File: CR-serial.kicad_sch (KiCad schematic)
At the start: 26 parts, among them J1 USB, J2 GPIO, J3 UART0, J4 UART1, J5 UART2, J6 UART3_HV, J7 RS232_0, J8 RS232_1, U1 CP2108-xxx-xM, U2 MAX232

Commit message: Make GPIO header double-row
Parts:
- J2: footprint Connector_PinHeader_2.54mm:PinHeader_1x16_P2.54mm_Vertical -> Connector_PinHeader_2.54mm:PinHeader_2x08_P2.54mm_Vertical
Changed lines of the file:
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@@
 			)
 		)
-		(property "Footprint" "Connector_PinHeader_2.54mm:PinHeader_1x16_P2.54mm_Vertical"
+		(property "Footprint" "Connector_PinHeader_2.54mm:PinHeader_2x08_P2.54mm_Vertical"
 			(at 67.31 118.11 0)
 			(effects

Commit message: Change RS232 connectors
Zones filled again
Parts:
- J7, J8: footprint Connector_PinHeader_2.54mm:PinHeader_1x03_P2.54mm_Vertical -> Connector_Phoenix_MC:PhoenixContact_MCV_1,5_3-G-3.81_1x03_P3.81mm_Vertical
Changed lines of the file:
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@@
 			)
 		)
-		(property "Footprint" "Connector_PinHeader_2.54mm:PinHeader_1x03_P2.54mm_Vertical"
+		(property "Footprint" "Connector_Phoenix_MC:PhoenixContact_MCV_1,5_3-G-3.81_1x03_P3.81mm_Vertical"
 			(at 259.08 88.9 0)
 			(effects
@@
 			)
 		)
-		(property "Footprint" "Connector_PinHeader_2.54mm:PinHeader_1x03_P2.54mm_Vertical"
+		(property "Footprint" "Connector_Phoenix_MC:PhoenixContact_MCV_1,5_3-G-3.81_1x03_P3.81mm_Vertical"
 			(at 259.08 101.6 0)
 			(effects

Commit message: Refactor UARTs: move GND next to TX/RX
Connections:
- net RX0: now also J3.3 (Pin_3); no longer J3.8 (Pin_8)
- net RX1: now also J4.3 (Pin_3); no longer J4.8 (Pin_8)
- net TX0: now also J3.2 (Pin_2); no longer J3.9 (Pin_9)
- net TX1: now also J4.2 (Pin_2); no longer J4.9 (Pin_9)
- net at U1.1 (RX3): now also J6.3 (Pin_3); no longer J6.8 (Pin_8)
- net at U1.10 (~{DTR3}): now also J6.6 (Pin_6); no longer J6.5 (Pin_5)
- net at U1.11 (~{RI2}): now also J5.9 (Pin_9); no longer J5.2 (Pin_2)
- net at U1.12 (~{DCD2}): now also J5.8 (Pin_8); no longer J5.3 (Pin_3)
- net at U1.13 (~{CTS2}): now also J5.5 (Pin_5); no longer J5.6 (Pin_6)
- net at U1.14 (~{RTS2}): now also J5.4 (Pin_4); no longer J5.7 (Pin_7)
- net at U1.15 (RX2): now also J5.3 (Pin_3); no longer J5.8 (Pin_8)
- net at U1.16 (TX2): now also J5.2 (Pin_2); no longer J5.9 (Pin_9)
- net at U1.17 (~{DSR2}): now also J5.7 (Pin_7); no longer J5.4 (Pin_4)
- net at U1.18 (~{DTR2}): now also J5.6 (Pin_6); no longer J5.5 (Pin_5)
- net at U1.4 (TX3): now also J6.2 (Pin_2); no longer J6.9 (Pin_9)
- net at U1.42 (~{RI1}): now also J4.9 (Pin_9); no longer J4.2 (Pin_2)
- net at U1.43 (~{DCD1}): now also J4.8 (Pin_8); no longer J4.3 (Pin_3)
- net at U1.44 (~{DSR1}): now also J4.7 (Pin_7); no longer J4.4 (Pin_4)
- net at U1.45 (~{DTR1}): now also J4.6 (Pin_6); no longer J4.5 (Pin_5)
- net at U1.46 (~{CTS1}): now also J4.5 (Pin_5); no longer J4.6 (Pin_6)
- net at U1.47 (~{RTS1}): now also J4.4 (Pin_4); no longer J4.7 (Pin_7)
- net at U1.5 (~{CTS3}): now also J6.5 (Pin_5); no longer J6.6 (Pin_6)
- net at U1.50 (~{RI0}): now also J3.9 (Pin_9); no longer J3.2 (Pin_2)
- net at U1.51 (~{DCD0}): now also J3.8 (Pin_8); no longer J3.3 (Pin_3)
- net at U1.52 (~{DSR0}): now also J3.7 (Pin_7); no longer J3.4 (Pin_4)
- net at U1.53 (~{DTR0}): now also J3.6 (Pin_6); no longer J3.5 (Pin_5)
- net at U1.54 (~{CTS0}): now also J3.5 (Pin_5); no longer J3.6 (Pin_6)
- net at U1.55 (~{RTS0}): now also J3.4 (Pin_4); no longer J3.7 (Pin_7)
- net at U1.6 (~{RTS3}): now also J6.4 (Pin_4); no longer J6.7 (Pin_7)
- net at U1.7 (~{RI3}): now also J6.9 (Pin_9); no longer J6.2 (Pin_2)
- net at U1.8 (~{DCD3}): now also J6.8 (Pin_8); no longer J6.3 (Pin_3)
- net at U1.9 (~{DSR3}): now also J6.7 (Pin_7); no longer J6.4 (Pin_4)
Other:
- moved on the sheet: J3, J4, J5, J6
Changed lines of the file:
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@@
 	(wire
 		(pts
-			(xy 153.67 46.99) (xy 133.35 46.99)
-		)
-		(stroke
-			(width 0)
-			(type default)
-		)
-	)
-	(wire
-		(pts
 			(xy 153.67 72.39) (xy 133.35 72.39)
 		)
@@
 	(wire
 		(pts
+			(xy 133.35 46.99) (xy 153.67 46.99)
+		)
+		(stroke
+			(width 0)
+			(type default)
+		)
+	)
+	(wire
+		(pts
 			(xy 153.67 49.53) (xy 133.35 49.53)
 		)
@@
 	(symbol
 		(lib_id "Connector:Conn_01x09_Pin")
-		(at 158.75 100.33 180)
+		(at 158.75 97.79 0)
+		(mirror y)
 		(unit 1)
 		(exclude_from_sim no)
@@
 		(fields_autoplaced yes)
 		(property "Reference" "J5"
-			(at 160.02 99.0599 0)
+			(at 160.02 99.0601 0)
 			(effects
 				(font
@@
 		)
 		(property "Value" "UART2"
-			(at 160.02 101.5999 0)
+			(at 160.02 96.5201 0)
 			(effects
 				(font
@@
 		)
 		(property "Footprint" "Connector_PinHeader_2.54mm:PinHeader_1x09_P2.54mm_Vertical"
-			(at 158.75 100.33 0)
+			(at 158.75 97.79 0)
 			(effects
 				(font
@@
 		)
 		(property "Datasheet" "~"
-			(at 158.75 100.33 0)
+			(at 158.75 97.79 0)
 			(effects
 				(font
@@
 		)
 		(property "Description" "Generic connector, single row, 01x09, script generated"
-			(at 158.75 100.33 0)
+			(at 158.75 97.79 0)
 			(effects
 				(font
@@
 	(symbol
 		(lib_id "power:GND")
-		(at 153.67 87.63 270)
+		(at 153.67 64.77 270)
 		(unit 1)
 		(exclude_from_sim no)
@@
 		(fields_autoplaced yes)
 		(property "Reference" "#PWR018"
-			(at 147.32 87.63 0)
+			(at 147.32 64.77 0)
 			(effects
 				(font
@@
 		)
 		(property "Value" "GND"
-			(at 149.86 87.6299 90)
+			(at 149.86 64.7699 90)
 			(effects
 				(font
@@
 		)
 		(property "Footprint" ""
-			(at 153.67 87.63 0)
+			(at 153.67 64.77 0)
 			(effects
 				(font
@@
 		)
 		(property "Datasheet" ""
-			(at 153.67 87.63 0)
+			(at 153.67 64.77 0)
 			(effects
 				(font
@@
 		)
 		(property "Description" "Power symbol creates a global label with name \"GND\" , ground"
-			(at 153.67 87.63 0)
+			(at 153.67 64.77 0)
 			(effects
 				(font
@@
 	(symbol
 		(lib_id "power:GND")
-		(at 153.67 133.35 270)
+		(at 153.67 110.49 270)
 		(unit 1)
 		(exclude_from_sim no)
@@
 		(fields_autoplaced yes)
 		(property "Reference" "#PWR020"
-			(at 147.32 133.35 0)
+			(at 147.32 110.49 0)
 			(effects
 				(font
@@
 		)
 		(property "Value" "GND"
-			(at 149.86 133.3499 90)
+			(at 149.86 110.4899 90)
 			(effects
 				(font
@@
 		)
 		(property "Footprint" ""
-			(at 153.67 133.35 0)
+			(at 153.67 110.49 0)
 			(effects
 				(font
@@
 		)
 		(property "Datasheet" ""
-			(at 153.67 133.35 0)
+			(at 153.67 110.49 0)
 			(effects
 				(font
@@
 		)
 		(property "Description" "Power symbol creates a global label with name \"GND\" , ground"
-			(at 153.67 133.35 0)
+			(at 153.67 110.49 0)
 			(effects
 				(font
@@
 	(symbol
 		(lib_id "power:GND")
-		(at 153.67 110.49 270)
+		(at 153.67 87.63 270)
 		(unit 1)
 		(exclude_from_sim no)
@@
 		(fields_autoplaced yes)
 		(property "Reference" "#PWR019"
-			(at 147.32 110.49 0)
+			(at 147.32 87.63 0)
 			(effects
 				(font
@@
 		)
 		(property "Value" "GND"
-			(at 149.86 110.4899 90)
+			(at 149.86 87.6299 90)
 			(effects
 				(font
@@
 		)
 		(property "Footprint" ""
-			(at 153.67 110.49 0)
+			(at 153.67 87.63 0)
 			(effects
 				(font
@@
 		)
 		(property "Datasheet" ""
-			(at 153.67 110.49 0)
+			(at 153.67 87.63 0)
 			(effects
 				(font
@@
 		)
 		(property "Description" "Power symbol creates a global label with name \"GND\" , ground"
-			(at 153.67 110.49 0)
+			(at 153.67 87.63 0)
 			(effects
 				(font
@@
 	(symbol
 		(lib_id "Connector:Conn_01x09_Pin")
-		(at 158.75 123.19 180)
+		(at 158.75 120.65 0)
+		(mirror y)
 		(unit 1)
 		(exclude_from_sim no)
@@
 		(fields_autoplaced yes)
 		(property "Reference" "J6"
-			(at 160.02 121.9199 0)
+			(at 160.02 121.9201 0)
 			(effects
 				(font
@@
 		)
 		(property "Value" "UART3_HV"
-			(at 160.02 124.4599 0)
+			(at 160.02 119.3801 0)
 			(effects
 				(font
@@
 		)
 		(property "Footprint" "Connector_PinHeader_2.54mm:PinHeader_1x09_P2.54mm_Vertical"
-			(at 158.75 123.19 0)
+			(at 158.75 120.65 0)
 			(effects
 				(font
@@
 		)
 		(property "Datasheet" "~"
-			(at 158.75 123.19 0)
+			(at 158.75 120.65 0)
 			(effects
 				(font
@@
 		)
 		(property "Description" "Generic connector, single row, 01x09, script generated"
-			(at 158.75 123.19 0)
+			(at 158.75 120.65 0)
 			(effects
 				(font
@@
 	(symbol
 		(lib_id "power:GND")
-		(at 153.67 64.77 270)
+		(at 153.67 41.91 270)
 		(unit 1)
 		(exclude_from_sim no)
@@
 		(fields_autoplaced yes)
 		(property "Reference" "#PWR017"
-			(at 147.32 64.77 0)
+			(at 147.32 41.91 0)
 			(effects
 				(font
@@
 		)
 		(property "Value" "GND"
-			(at 149.86 64.7699 90)
+			(at 149.86 41.9099 90)
 			(effects
 				(font
@@
 		)
 		(property "Footprint" ""
-			(at 153.67 64.77 0)
+			(at 153.67 41.91 0)
 			(effects
 				(font
@@
 		)
 		(property "Datasheet" ""
-			(at 153.67 64.77 0)
+			(at 153.67 41.91 0)
 			(effects
 				(font
@@
 		)
 		(property "Description" "Power symbol creates a global label with name \"GND\" , ground"
-			(at 153.67 64.77 0)
+			(at 153.67 41.91 0)
 			(effects
 				(font
@@
 	(symbol
 		(lib_id "Connector:Conn_01x09_Pin")
-		(at 158.75 54.61 180)
+		(at 158.75 52.07 0)
+		(mirror y)
 		(unit 1)
 		(exclude_from_sim no)
@@
 		(fields_autoplaced yes)
 		(property "Reference" "J3"
-			(at 160.02 53.3399 0)
+			(at 160.02 53.3401 0)
 			(effects
 				(font
@@
 		)
 		(property "Value" "UART0"
-			(at 160.02 55.8799 0)
+			(at 160.02 50.8001 0)
 			(effects
 				(font
@@
 		)
 		(property "Footprint" "Connector_PinHeader_2.54mm:PinHeader_1x09_P2.54mm_Vertical"
-			(at 158.75 54.61 0)
+			(at 158.75 52.07 0)
 			(effects
 				(font
@@
 		)
 		(property "Datasheet" "~"
-			(at 158.75 54.61 0)
+			(at 158.75 52.07 0)
 			(effects
 				(font
@@
 		)
 		(property "Description" "Generic connector, single row, 01x09, script generated"
-			(at 158.75 54.61 0)
+			(at 158.75 52.07 0)
 			(effects
 				(font
@@
 	(symbol
 		(lib_id "Connector:Conn_01x09_Pin")
-		(at 158.75 77.47 180)
+		(at 158.75 74.93 0)
+		(mirror y)
 		(unit 1)
 		(exclude_from_sim no)
@@
 		(fields_autoplaced yes)
 		(property "Reference" "J4"
-			(at 160.02 76.1999 0)
+			(at 160.02 76.2001 0)
 			(effects
 				(font
@@
 		)
 		(property "Value" "UART1"
-			(at 160.02 78.7399 0)
+			(at 160.02 73.6601 0)
 			(effects
 				(font
@@
 		)
 		(property "Footprint" "Connector_PinHeader_2.54mm:PinHeader_1x09_P2.54mm_Vertical"
-			(at 158.75 77.47 0)
+			(at 158.75 74.93 0)
 			(effects
 				(font
@@
 		)
 		(property "Datasheet" "~"
-			(at 158.75 77.47 0)
+			(at 158.75 74.93 0)
 			(effects
 				(font
@@
 		)
 		(property "Description" "Generic connector, single row, 01x09, script generated"
-			(at 158.75 77.47 0)
+			(at 158.75 74.93 0)
 			(effects
 				(font

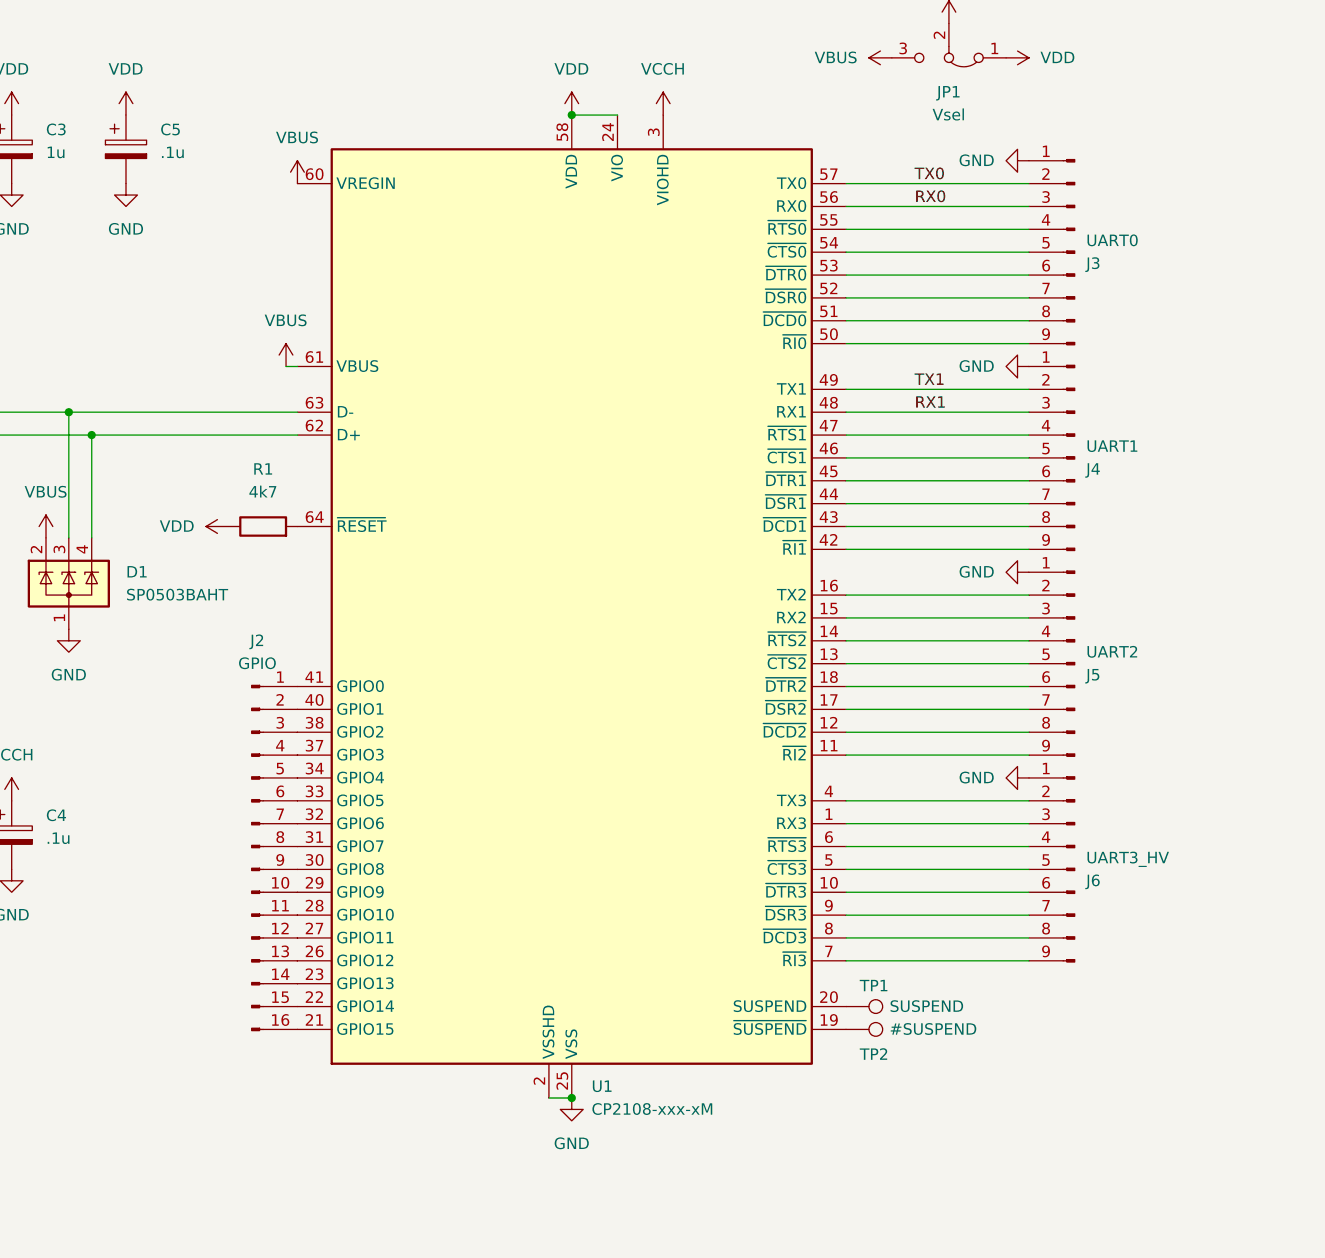
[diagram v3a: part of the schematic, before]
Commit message: Add 0Rs on all CP2108 outputs
`--patience` is recommended
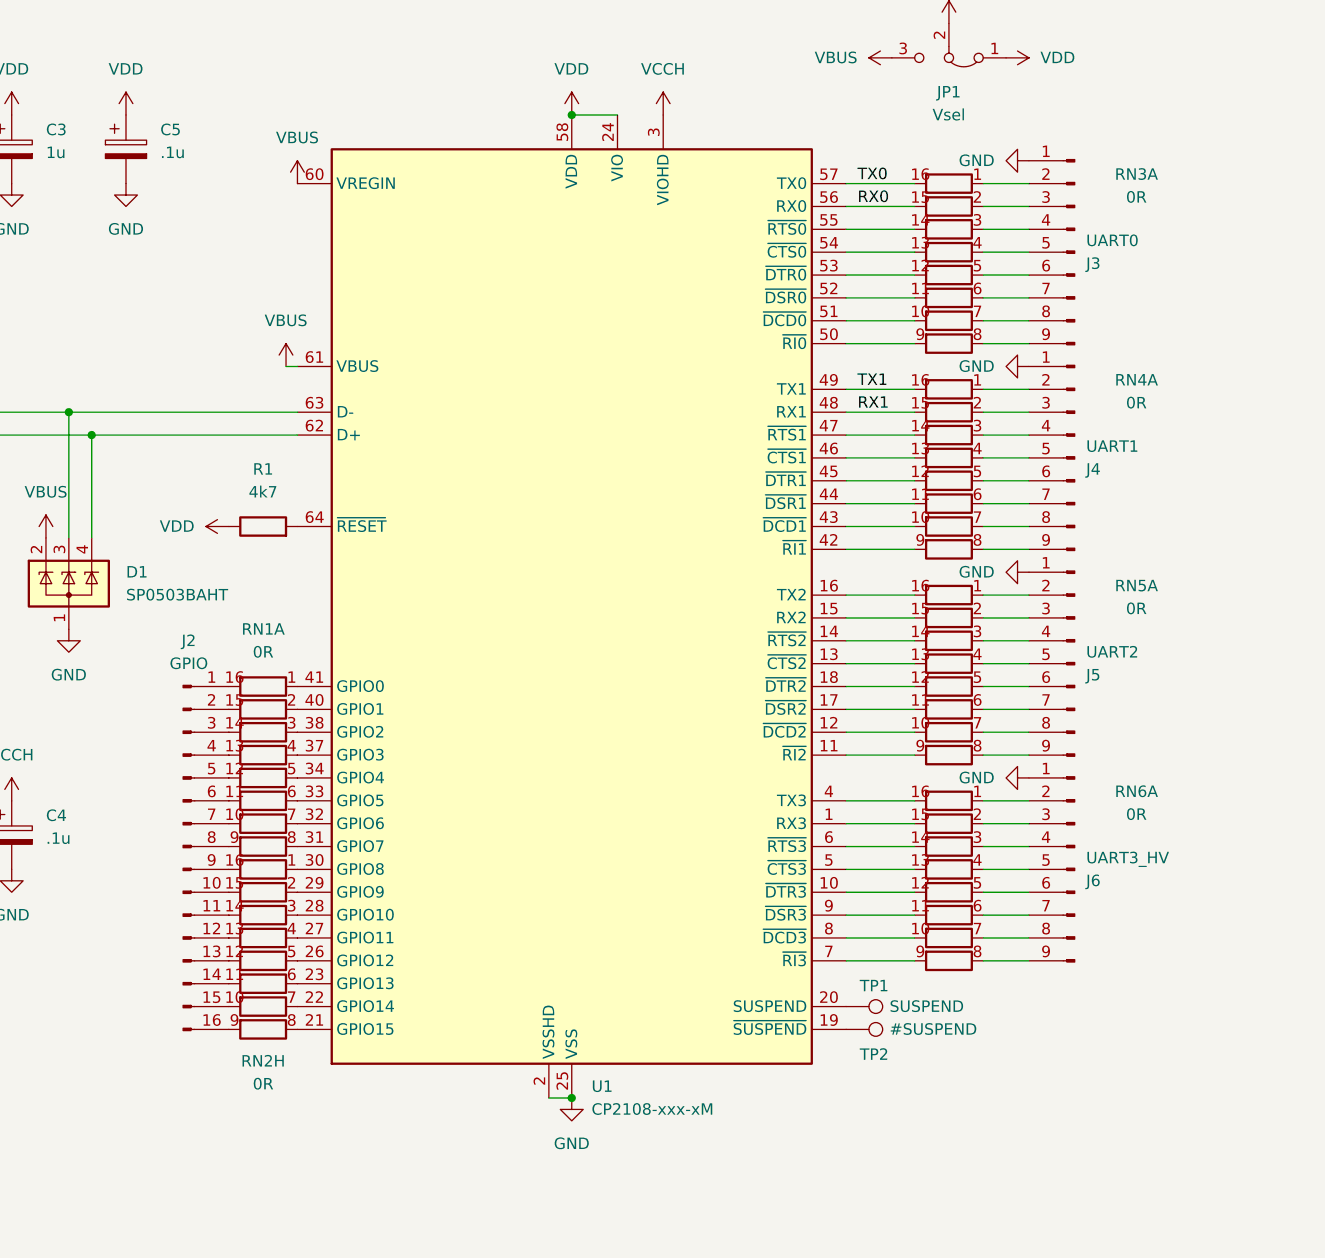
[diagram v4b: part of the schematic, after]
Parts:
- added RN1, RN2, RN3, RN4, RN5, RN6: 0R, Resistor_SMD:R_Array_Convex_8x0602, symbol Device:R_Pack08_Split
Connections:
- net RX0: now also RN3.15 (R2.2); no longer J3.3 (Pin_3)
- net RX1: now also RN4.15 (R2.2); no longer J4.3 (Pin_3)
- net TX0: now also RN3.16 (R1.2); no longer J3.2 (Pin_2)
- net TX1: now also RN4.16 (R1.2); no longer J4.2 (Pin_2)
- net at U1.1 (RX3): now also RN6.15 (R2.2); no longer J6.3 (Pin_3)
- net at U1.10 (~{DTR3}): now also RN6.12 (R5.2); no longer J6.6 (Pin_6)
- net at U1.11 (~{RI2}): now also RN5.9 (R8.2); no longer J5.9 (Pin_9)
- net at U1.12 (~{DCD2}): now also RN5.10 (R7.2); no longer J5.8 (Pin_8)
- net at U1.13 (~{CTS2}): now also RN5.13 (R4.2); no longer J5.5 (Pin_5)
- net at U1.14 (~{RTS2}): now also RN5.14 (R3.2); no longer J5.4 (Pin_4)
- net at U1.15 (RX2): now also RN5.15 (R2.2); no longer J5.3 (Pin_3)
- net at U1.16 (TX2): now also RN5.16 (R1.2); no longer J5.2 (Pin_2)
- net at U1.17 (~{DSR2}): now also RN5.11 (R6.2); no longer J5.7 (Pin_7)
- net at U1.18 (~{DTR2}): now also RN5.12 (R5.2); no longer J5.6 (Pin_6)
- net at U1.21 (GPIO15): now also RN2.8 (R8.1); no longer J2.16 (Pin_16)
- net at U1.22 (GPIO14): now also RN2.7 (R7.1); no longer J2.15 (Pin_15)
- net at U1.23 (GPIO13): now also RN2.6 (R6.1); no longer J2.14 (Pin_14)
- net at U1.26 (GPIO12): now also RN2.5 (R5.1); no longer J2.13 (Pin_13)
- net at U1.27 (GPIO11): now also RN2.4 (R4.1); no longer J2.12 (Pin_12)
- net at U1.28 (GPIO10): now also RN2.3 (R3.1); no longer J2.11 (Pin_11)
- net at U1.29 (GPIO9): now also RN2.2 (R2.1); no longer J2.10 (Pin_10)
- net at U1.30 (GPIO8): now also RN2.1 (R1.1); no longer J2.9 (Pin_9)
- net at U1.31 (GPIO7): now also RN1.8 (R8.1); no longer J2.8 (Pin_8)
- net at U1.32 (GPIO6): now also RN1.7 (R7.1); no longer J2.7 (Pin_7)
- net at U1.33 (GPIO5): now also RN1.6 (R6.1); no longer J2.6 (Pin_6)
- net at U1.34 (GPIO4): now also RN1.5 (R5.1); no longer J2.5 (Pin_5)
- net at U1.37 (GPIO3): now also RN1.4 (R4.1); no longer J2.4 (Pin_4)
- net at U1.38 (GPIO2): now also RN1.3 (R3.1); no longer J2.3 (Pin_3)
- net at U1.4 (TX3): now also RN6.16 (R1.2); no longer J6.2 (Pin_2)
- net at U1.40 (GPIO1): now also RN1.2 (R2.1); no longer J2.2 (Pin_2)
- net at U1.41 (GPIO0): now also RN1.1 (R1.1); no longer J2.1 (Pin_1)
- net at U1.42 (~{RI1}): now also RN4.9 (R8.2); no longer J4.9 (Pin_9)
- net at U1.43 (~{DCD1}): now also RN4.10 (R7.2); no longer J4.8 (Pin_8)
- net at U1.44 (~{DSR1}): now also RN4.11 (R6.2); no longer J4.7 (Pin_7)
- net at U1.45 (~{DTR1}): now also RN4.12 (R5.2); no longer J4.6 (Pin_6)
- net at U1.46 (~{CTS1}): now also RN4.13 (R4.2); no longer J4.5 (Pin_5)
- net at U1.47 (~{RTS1}): now also RN4.14 (R3.2); no longer J4.4 (Pin_4)
- net at U1.5 (~{CTS3}): now also RN6.13 (R4.2); no longer J6.5 (Pin_5)
- net at U1.50 (~{RI0}): now also RN3.9 (R8.2); no longer J3.9 (Pin_9)
- net at U1.51 (~{DCD0}): now also RN3.10 (R7.2); no longer J3.8 (Pin_8)
- net at U1.52 (~{DSR0}): now also RN3.11 (R6.2); no longer J3.7 (Pin_7)
- net at U1.53 (~{DTR0}): now also RN3.12 (R5.2); no longer J3.6 (Pin_6)
- net at U1.54 (~{CTS0}): now also RN3.13 (R4.2); no longer J3.5 (Pin_5)
- net at U1.55 (~{RTS0}): now also RN3.14 (R3.2); no longer J3.4 (Pin_4)
- net at U1.6 (~{RTS3}): now also RN6.14 (R3.2); no longer J6.4 (Pin_4)
- net at U1.7 (~{RI3}): now also RN6.9 (R8.2); no longer J6.9 (Pin_9)
- net at U1.8 (~{DCD3}): now also RN6.10 (R7.2); no longer J6.8 (Pin_8)
- net at U1.9 (~{DSR3}): now also RN6.11 (R6.2); no longer J6.7 (Pin_7)
- new net: J4.5 (Pin_5), RN4.4 (R4.1)
- new net: J5.2 (Pin_2), RN5.1 (R1.1)
- new net: J3.8 (Pin_8), RN3.7 (R7.1)
- new net: J2.1 (Pin_1), RN1.16 (R1.2)
- new net: J2.13 (Pin_13), RN2.12 (R5.2)
- new net: J6.9 (Pin_9), RN6.8 (R8.1)
- new net: J4.6 (Pin_6), RN4.5 (R5.1)
- new net: J5.3 (Pin_3), RN5.2 (R2.1)
- new net: J5.4 (Pin_4), RN5.3 (R3.1)
- new net: J5.5 (Pin_5), RN5.4 (R4.1)
- new net: J5.6 (Pin_6), RN5.5 (R5.1)
- new net: J5.7 (Pin_7), RN5.6 (R6.1)
- new net: J5.8 (Pin_8), RN5.7 (R7.1)
- new net: J5.9 (Pin_9), RN5.8 (R8.1)
- new net: J2.10 (Pin_10), RN2.15 (R2.2)
- new net: J2.4 (Pin_4), RN1.13 (R4.2)
- new net: J6.7 (Pin_7), RN6.6 (R6.1)
- new net: J6.2 (Pin_2), RN6.1 (R1.1)
- new net: J6.3 (Pin_3), RN6.2 (R2.1)
- new net: J6.4 (Pin_4), RN6.3 (R3.1)
- new net: J6.5 (Pin_5), RN6.4 (R4.1)
- new net: J6.6 (Pin_6), RN6.5 (R5.1)
- new net: J6.8 (Pin_8), RN6.7 (R7.1)
- new net: J2.16 (Pin_16), RN2.9 (R8.2)
- new net: J3.3 (Pin_3), RN3.2 (R2.1)
- new net: J2.12 (Pin_12), RN2.13 (R4.2)
- new net: J3.7 (Pin_7), RN3.6 (R6.1)
- new net: J3.2 (Pin_2), RN3.1 (R1.1)
- new net: J3.4 (Pin_4), RN3.3 (R3.1)
- new net: J3.5 (Pin_5), RN3.4 (R4.1)
- new net: J3.6 (Pin_6), RN3.5 (R5.1)
- new net: J3.9 (Pin_9), RN3.8 (R8.1)
- new net: J4.8 (Pin_8), RN4.7 (R7.1)
- new net: J4.2 (Pin_2), RN4.1 (R1.1)
- new net: J4.3 (Pin_3), RN4.2 (R2.1)
- new net: J4.4 (Pin_4), RN4.3 (R3.1)
- new net: J4.7 (Pin_7), RN4.6 (R6.1)
- new net: J4.9 (Pin_9), RN4.8 (R8.1)
- new net: J2.14 (Pin_14), RN2.11 (R6.2)
- new net: J2.9 (Pin_9), RN2.16 (R1.2)
- new net: J2.3 (Pin_3), RN1.14 (R3.2)
- new net: J2.6 (Pin_6), RN1.11 (R6.2)
- new net: J2.15 (Pin_15), RN2.10 (R7.2)
- new net: J2.5 (Pin_5), RN1.12 (R5.2)
- new net: J2.8 (Pin_8), RN1.9 (R8.2)
- new net: J2.7 (Pin_7), RN1.10 (R7.2)
- new net: J2.11 (Pin_11), RN2.14 (R3.2)
- new net: J2.2 (Pin_2), RN1.15 (R2.2)
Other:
- moved on the sheet: J2
